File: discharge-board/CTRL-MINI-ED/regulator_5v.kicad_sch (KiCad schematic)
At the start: 3 parts, among them U7 BD33FC0FP

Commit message: Cleanup old powers
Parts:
- removed U7: BD33FC0FP, Package_TO_SOT_SMD:TO-252-2, symbol Regulator_Linear:BD33FC0FP
- added U7: BD50FC0FP, Package_TO_SOT_SMD:TO-252-2, symbol Regulator_Linear:BD50FC0FP
- renumbered C36 to C35, C37 to C36
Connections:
- net GND: now also U7.2 (GND)
- net VIN: now also U7.1 (VCC)
- net VOUT: now also U7.3 (VO)
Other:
- note added: "RATING Input: ~25V Output: 5V, 1A"
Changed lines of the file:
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@@
+		)
+	)
+	(text "RATING\nInput: ~25V\nOutput: 5V, 1A\n"
+		(exclude_from_sim no)
+		(at 81.28 38.354 0)
+		(effects
+			(font
+				(size 1.27 1.27)
+			)
+			(justify left)
 		)
 	)
@@
 		(instances
 			(project "CTRL-MINI-ED"
-				(path "/3fa1ca74-4d0d-40dd-8b5c-0d4be11bd5b5/a9794609-42db-49f0-aeeb-4c313a94f296"
+				(path "/3fa1ca74-4d0d-40dd-8b5c-0d4be11bd5b5/4aad0038-914a-49e5-b2b1-142b86064ddf"
 					(reference "#PWR046")
 					(unit 1)
@@
 	)
 	(symbol
-		(lib_id "Regulator_Linear:BD33FC0FP")
+		(lib_id "Regulator_Linear:BD50FC0FP")
 		(at 87.63 54.61 0)
 		(unit 1)
@@
 			)
 		)
-		(property "Value" "BD33FC0FP"
+		(property "Value" "BD50FC0FP"
 			(at 87.63 50.8 0)
 			(effects
@@
 			)
 		)
-		(property "Description" "1A, 3.3V LDO regulator with OVP & TSP, without enable, TO-252"
+		(property "Description" "1A, 5.0V LDO regulator with OVP & TSP, without enable, TO-252"
 			(at 87.63 54.61 0)
 			(effects
@@
 			)
 		)
-		(property "LCSC" "C2846670"
+		(property "LCSC" "C920705"
 			(at 87.63 54.61 0)
 			(effects
@@
 			)
 		)
+		(pin "1"
+		)
+		(pin "3"
+		)
 		(pin "2"
-		)
-		(pin "1"
-		)
-		(pin "3"
 		)
 		(instances
 			(project ""
-				(path "/3fa1ca74-4d0d-40dd-8b5c-0d4be11bd5b5/a9794609-42db-49f0-aeeb-4c313a94f296"
+				(path "/3fa1ca74-4d0d-40dd-8b5c-0d4be11bd5b5/4aad0038-914a-49e5-b2b1-142b86064ddf"
 					(reference "U7")
 					(unit 1)
@@
 		(on_board yes)
 		(dnp no)
-		(property "Reference" "C36"
+		(property "Reference" "C35"
 			(at 75.946 59.944 0)
 			(effects
@@
 		(instances
 			(project "CTRL-MINI-ED"
-				(path "/3fa1ca74-4d0d-40dd-8b5c-0d4be11bd5b5/a9794609-42db-49f0-aeeb-4c313a94f296"
-					(reference "C36")
+				(path "/3fa1ca74-4d0d-40dd-8b5c-0d4be11bd5b5/4aad0038-914a-49e5-b2b1-142b86064ddf"
+					(reference "C35")
 					(unit 1)
 				)
@@
 		(on_board yes)
 		(dnp no)
-		(property "Reference" "C37"
+		(property "Reference" "C36"
 			(at 102.616 59.944 0)
 			(effects
@@
 		(instances
 			(project "CTRL-MINI-ED"
-				(path "/3fa1ca74-4d0d-40dd-8b5c-0d4be11bd5b5/a9794609-42db-49f0-aeeb-4c313a94f296"
-					(reference "C37")
+				(path "/3fa1ca74-4d0d-40dd-8b5c-0d4be11bd5b5/4aad0038-914a-49e5-b2b1-142b86064ddf"
+					(reference "C36")
 					(unit 1)
 				)

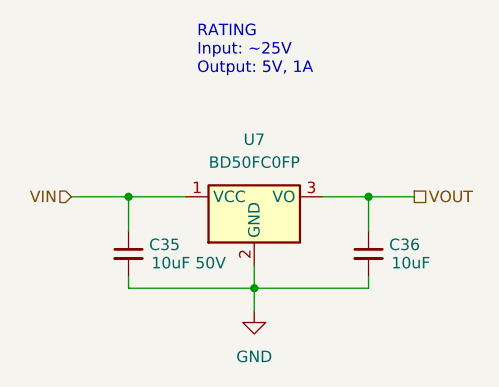
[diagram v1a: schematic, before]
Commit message: Basic building block layout
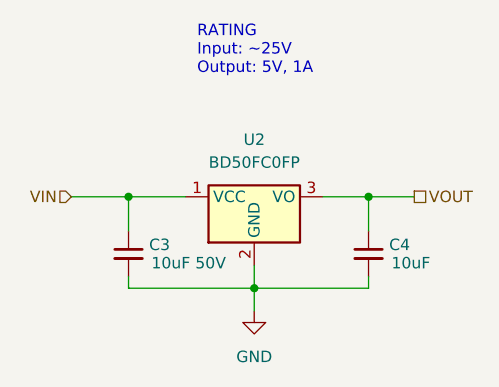
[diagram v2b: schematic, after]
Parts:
- renumbered C35 to C3, C36 to C4, U7 to U2
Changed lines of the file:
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@@
 		(dnp no)
 		(fields_autoplaced yes)
-		(property "Reference" "#PWR046"
+		(property "Reference" "#PWR019"
 			(at 87.63 73.66 0)
 			(effects
@@
 			(project "CTRL-MINI-ED"
 				(path "/3fa1ca74-4d0d-40dd-8b5c-0d4be11bd5b5/4aad0038-914a-49e5-b2b1-142b86064ddf"
-					(reference "#PWR046")
+					(reference "#PWR019")
 					(unit 1)
 				)
@@
 		(dnp no)
 		(fields_autoplaced yes)
-		(property "Reference" "U7"
+		(property "Reference" "U2"
 			(at 87.63 48.26 0)
 			(effects
@@
 			(project ""
 				(path "/3fa1ca74-4d0d-40dd-8b5c-0d4be11bd5b5/4aad0038-914a-49e5-b2b1-142b86064ddf"
-					(reference "U7")
+					(reference "U2")
 					(unit 1)
 				)
@@
 		(on_board yes)
 		(dnp no)
-		(property "Reference" "C35"
+		(property "Reference" "C3"
 			(at 75.946 59.944 0)
 			(effects
@@
 			(project "CTRL-MINI-ED"
 				(path "/3fa1ca74-4d0d-40dd-8b5c-0d4be11bd5b5/4aad0038-914a-49e5-b2b1-142b86064ddf"
-					(reference "C35")
+					(reference "C3")
 					(unit 1)
 				)
@@
 		(on_board yes)
 		(dnp no)
-		(property "Reference" "C36"
+		(property "Reference" "C4"
 			(at 102.616 59.944 0)
 			(effects
@@
 			(project "CTRL-MINI-ED"
 				(path "/3fa1ca74-4d0d-40dd-8b5c-0d4be11bd5b5/4aad0038-914a-49e5-b2b1-142b86064ddf"
-					(reference "C36")
+					(reference "C4")
 					(unit 1)
 				)
